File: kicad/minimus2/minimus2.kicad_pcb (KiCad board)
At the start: 2 copper layers, 67.7 x 58.8 mm, 84 parts, among them J1 PROG_SER, J2 LM, J3 LM, Q1 SSM6N58NU_LF, Q2 SSM6N58NU_LF, Q3 DMN3051L, SW1 RESET, SW2 USER_A, SW4 SW_SPDT, U1 LSM6DSRTR, U2 STM32U575CITx, U3 DRV8835, U4 AS5047D, U5 AS5047D, U6 AP2210N-3.3TRG1, U9 AP7370-50FDC

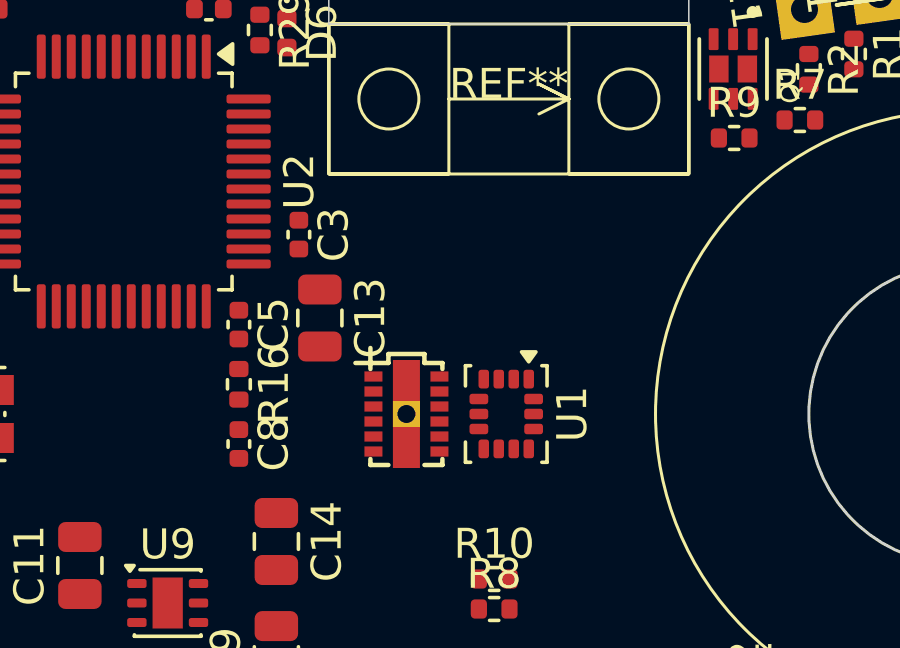
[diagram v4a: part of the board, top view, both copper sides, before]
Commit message: update the motor mounts
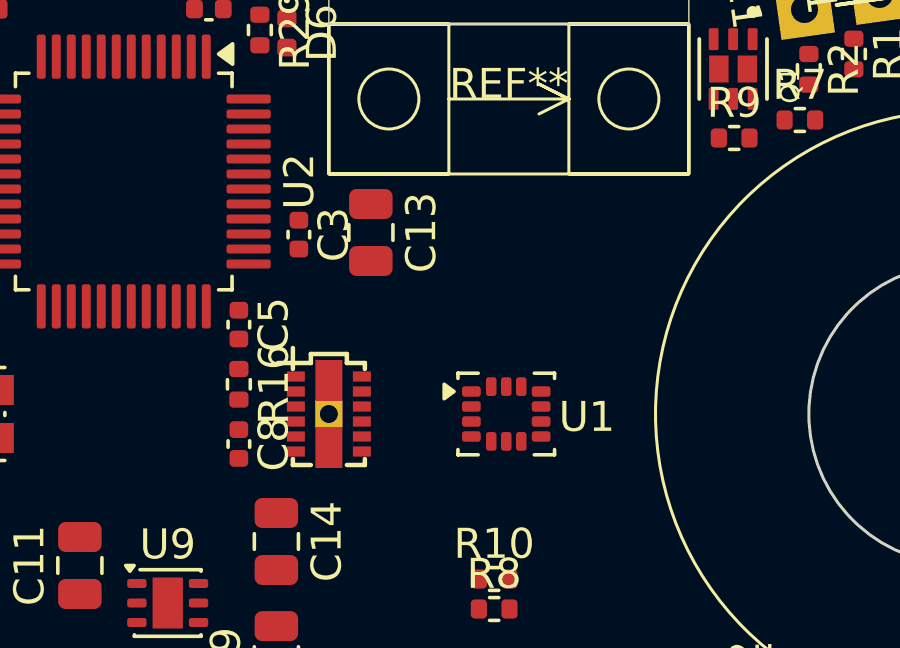
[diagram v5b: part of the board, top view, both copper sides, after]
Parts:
- moved C13 3.32 mm to (95.4, 94.0)
- moved U3 2.58 mm to (94.0, 100.0)
- turned U1 to 0 degrees
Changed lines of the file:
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@@
 		)
 		(embedded_fonts no)
-		(model "${KIPRJMOD}/libraries/minimus.3dshape/MotorMountMK4_TYRE_v4_LHS.step"
+		(model "${KIPRJMOD}/libraries/minimus.3dshape/MotorMountMK4_Thin_LHS.step"
 			(offset
 				(xyz 0 -2.5 0)
@@
 	(footprint "Capacitor_SMD:C_0805_2012Metric"
 		(layer "F.Cu")
-		(at 93.7 96.8 -90)
+		(at 95.4 93.95 -90)
 		(descr "Capacitor SMD 0805 (2012 Metric), square (rectangular) end terminal, IPC-7351 nominal, (Body size source: IPC-SM-782 page 76, https://www.pcb-3d.com/wordpress/wp-content/uploads/ipc-sm-782a_amendment_1_and_2.pdf, https://docs.google.com/spreadsheets/d/1BsfQQcO9C6DZCsRaXUlFlo91Tg2WpOkGARC1WS5S8t0/edit?usp=sharing), generated with kicad-footprint-generator")
 		(tags "capacitor")
@@
 			(stroke
 				(width 0.1)
-				(type default)
+				(type solid)
 			)
 			(layer "F.SilkS")
@@
 		)
 		(embedded_fonts no)
-		(model "${KIPRJMOD}/libraries/minimus.3dshape/MotorMountMK4_TYRE_v4_RHS.step"
+		(model "${KIPRJMOD}/libraries/minimus.3dshape/MotorMountMK4_Thin_RHS.step"
 			(offset
 				(xyz 0 2.5 0)
@@
 	(footprint "Package_LGA:LGA-14_3x2.5mm_P0.5mm_LayoutBorder3x4y"
 		(layer "F.Cu")
-		(at 99.9125 100 -90)
+		(at 99.9125 100)
 		(descr "LGA, 14 Pin (https://www.st.com/resource/en/datasheet/lsm6ds3tr-c.pdf), generated with kicad-footprint-generator ipc_noLead_generator.py")
 		(tags "LGA NoLead")
 		(property "Reference" "U1"
-			(at 0 -2.2 90)
+			(at 2.6875 0.1 0)
 			(layer "F.SilkS")
 			(effects
@@
 		)
 		(property "Value" "LSM6DSRTR"
-			(at 0 2.2 90)
+			(at 0 2.2 0)
 			(layer "F.Fab")
 			(effects
@@
 		)
 		(property "Datasheet" "https://www.st.com/resource/en/datasheet/lsm6ds3tr-c.pdf"
-			(at 0 0 90)
+			(at 0 0 0)
 			(layer "F.Fab")
 			(hide yes)
@@
 		)
 		(property "Description" "I2C/SPI, iNEMO inertial module: always-on 3D accelerometer and 3D gyroscope"
-			(at 0 0 90)
+			(at 0 0 0)
 			(layer "F.Fab")
 			(hide yes)
@@
 		)
 		(property "LCSC" "C784817"
-			(at 0 0 270)
+			(at 0 0 0)
 			(unlocked yes)
 			(layer "F.Fab")
@@
 		)
 		(property "Digikey" "-"
-			(at 0 0 270)
+			(at 0 0 0)
 			(unlocked yes)
 			(layer "F.Fab")
@@
 		(attr smd)
 		(fp_line
-			(start -1.61 1.36)
-			(end -1.61 1.185)
+			(start -1.61 -1.36)
+			(end -0.935 -1.36)
 			(stroke
 				(width 0.12)
@@
 		)
 		(fp_line
-			(start -0.935 1.36)
-			(end -1.61 1.36)
+			(start -1.61 -1.185)
+			(end -1.61 -1.36)
 			(stroke
 				(width 0.12)
@@
 		)
 		(fp_line
-			(start 1.61 1.36)
-			(end 0.935 1.36)
+			(start -1.61 1.36)
+			(end -1.61 1.185)
 			(stroke
 				(width 0.12)
@@
 		)
 		(fp_line
-			(start 1.61 1.185)
-			(end 1.61 1.36)
+			(start -0.935 1.36)
+			(end -1.61 1.36)
 			(stroke
 				(width 0.12)
@@
 		)
 		(fp_line
-			(start -1.61 -1.185)
-			(end -1.61 -1.36)
+			(start 0.935 -1.36)
+			(end 1.61 -1.36)
 			(stroke
 				(width 0.12)
@@
 		)
 		(fp_line
-			(start -1.61 -1.36)
-			(end -0.935 -1.36)
+			(start 1.61 -1.36)
+			(end 1.61 -1.185)
 			(stroke
 				(width 0.12)
@@
 		)
 		(fp_line
-			(start 0.935 -1.36)
-			(end 1.61 -1.36)
+			(start 1.61 1.185)
+			(end 1.61 1.36)
 			(stroke
 				(width 0.12)
@@
 		)
 		(fp_line
-			(start 1.61 -1.36)
-			(end 1.61 -1.185)
+			(start 1.61 1.36)
+			(end 0.935 1.36)
 			(stroke
 				(width 0.12)
@@
 		)
 		(fp_text user "${REFERENCE}"
-			(at 0 0 90)
+			(at 0 0 0)
 			(layer "F.Fab")
 			(effects
@@
 		)
 		(pad "1" smd roundrect
-			(at -1.1625 -0.75 270)
+			(at -1.1625 -0.75)
 			(size 0.625 0.35)
 			(layers "F.Cu" "F.Mask" "F.Paste")
@@
 		)
 		(pad "2" smd roundrect
-			(at -1.1625 -0.25 270)
+			(at -1.1625 -0.25)
 			(size 0.625 0.35)
 			(layers "F.Cu" "F.Mask" "F.Paste")
@@
 		)
 		(pad "3" smd roundrect
-			(at -1.1625 0.25 270)
+			(at -1.1625 0.25)
 			(size 0.625 0.35)
 			(layers "F.Cu" "F.Mask" "F.Paste")
@@
 		)
 		(pad "4" smd roundrect
-			(at -1.1625 0.75 270)
+			(at -1.1625 0.75)
 			(size 0.625 0.35)
 			(layers "F.Cu" "F.Mask" "F.Paste")
@@
 		)
 		(pad "5" smd roundrect
-			(at -0.5 0.9125 270)
+			(at -0.5 0.9125)
 			(size 0.35 0.625)
 			(layers "F.Cu" "F.Mask" "F.Paste")
@@
 		)
 		(pad "6" smd roundrect
-			(at 0 0.9125 270)
+			(at 0 0.9125)
 			(size 0.35 0.625)
 			(layers "F.Cu" "F.Mask" "F.Paste")
@@
 		)
 		(pad "7" smd roundrect
-			(at 0.5 0.9125 270)
+			(at 0.5 0.9125)
 			(size 0.35 0.625)
 			(layers "F.Cu" "F.Mask" "F.Paste")
@@
 		)
 		(pad "8" smd roundrect
-			(at 1.1625 0.75 270)
+			(at 1.1625 0.75)
 			(size 0.625 0.35)
 			(layers "F.Cu" "F.Mask" "F.Paste")
@@
 		)
 		(pad "9" smd roundrect
-			(at 1.1625 0.25 270)
+			(at 1.1625 0.25)
 			(size 0.625 0.35)
 			(layers "F.Cu" "F.Mask" "F.Paste")
@@
 		)
 		(pad "10" smd roundrect
-			(at 1.1625 -0.25 270)
+			(at 1.1625 -0.25)
 			(size 0.625 0.35)
 			(layers "F.Cu" "F.Mask" "F.Paste")
@@
 		)
 		(pad "11" smd roundrect
-			(at 1.1625 -0.75 270)
+			(at 1.1625 -0.75)
 			(size 0.625 0.35)
 			(layers "F.Cu" "F.Mask" "F.Paste")
@@
 		)
 		(pad "12" smd roundrect
-			(at 0.5 -0.9125 270)
+			(at 0.5 -0.9125)
 			(size 0.35 0.625)
 			(layers "F.Cu" "F.Mask" "F.Paste")
@@
 		)
 		(pad "13" smd roundrect
-			(at 0 -0.9125 270)
+			(at 0 -0.9125)
 			(size 0.35 0.625)
 			(layers "F.Cu" "F.Mask" "F.Paste")
@@
 		)
 		(pad "14" smd roundrect
-			(at -0.5 -0.9125 270)
+			(at -0.5 -0.9125)
 			(size 0.35 0.625)
 			(layers "F.Cu" "F.Mask" "F.Paste")
@@
 		(placed yes)
 		(layer "F.Cu")
-		(at 96.585 100 -90)
+		(at 94 100 -90)
 		(property "Reference" "U3"
 			(at 3 -2 90)

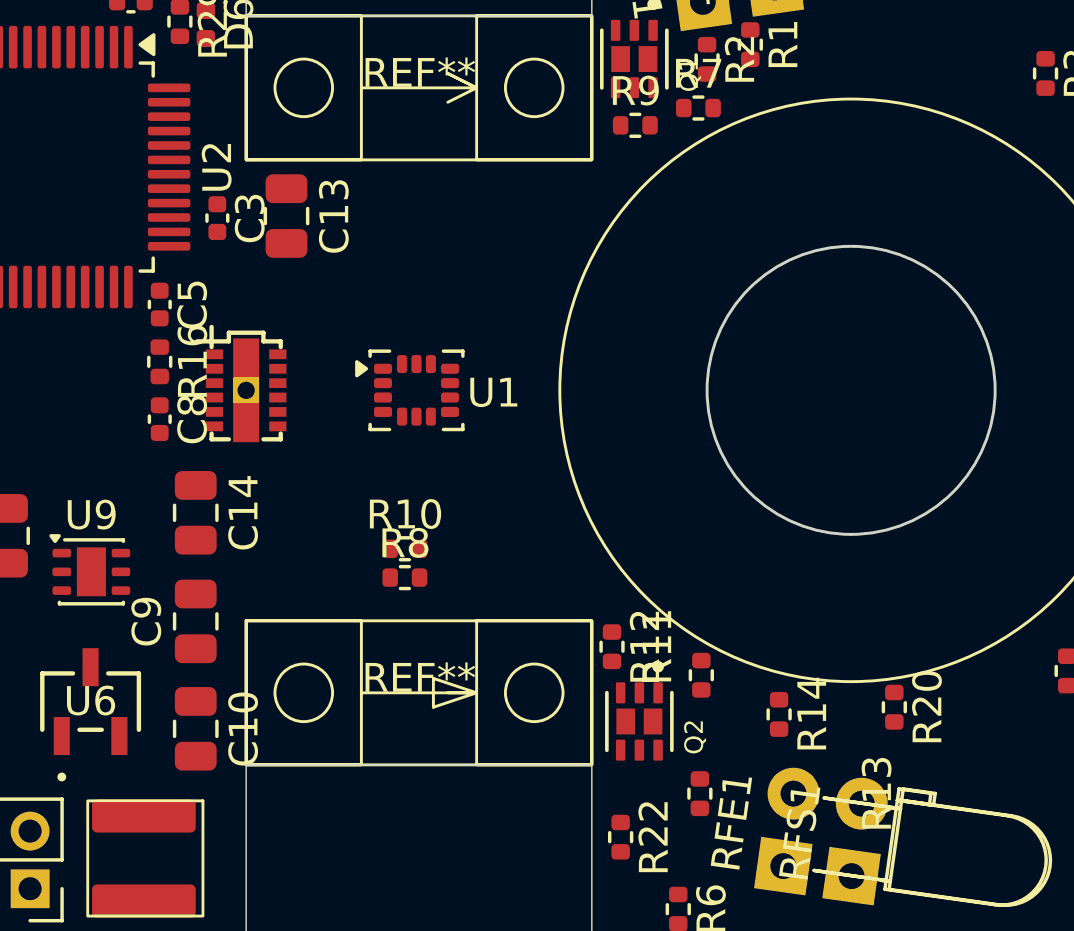
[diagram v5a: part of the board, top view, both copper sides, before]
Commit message: add guideline graduations to silkscreen
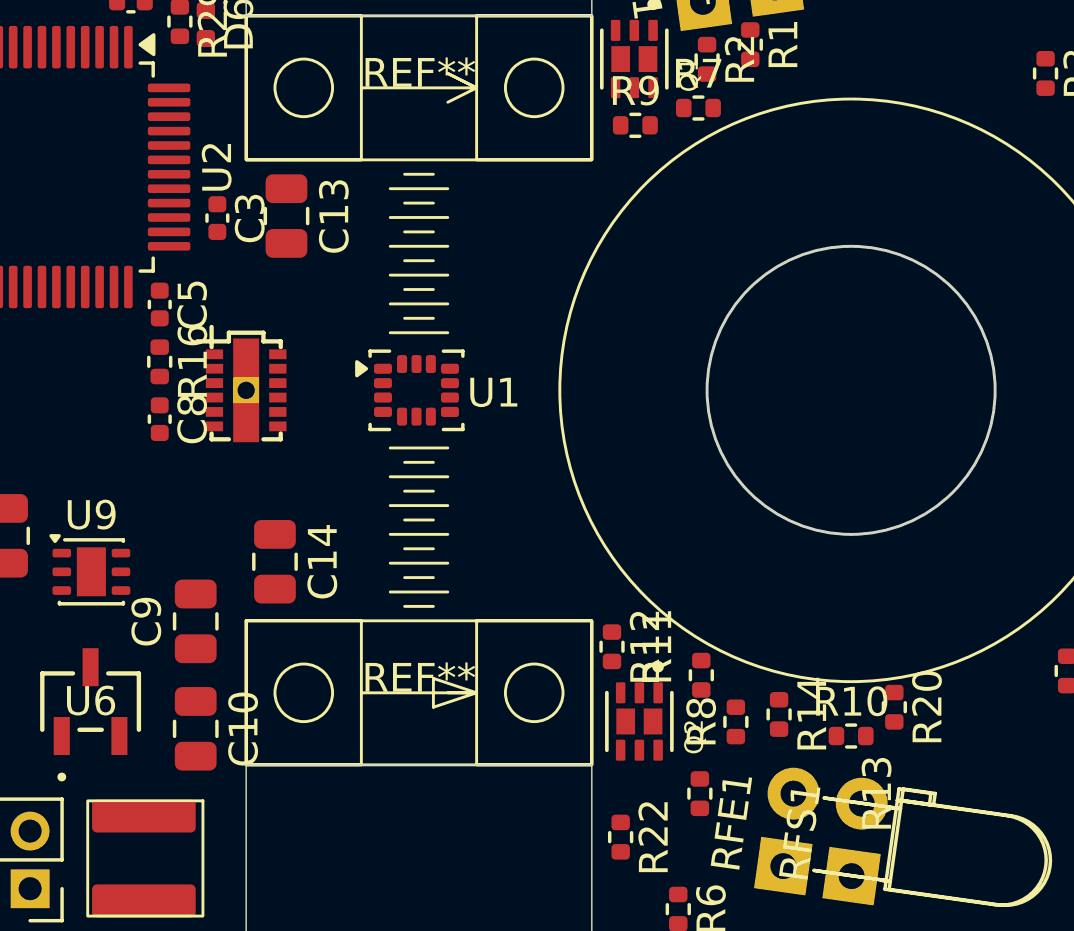
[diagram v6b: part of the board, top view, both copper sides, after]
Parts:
- moved R10 16.8 mm to (115.0, 112.0)
- moved R8 12.5 mm to (111.0, 111.5), turned to 90 degrees
- moved C14 3.23 mm to (95.0, 106.0)
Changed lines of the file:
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@@
 	(footprint "Capacitor_SMD:C_0805_2012Metric"
 		(layer "F.Cu")
-		(at 92.25 104.25 -90)
+		(at 95 105.95 -90)
 		(descr "Capacitor SMD 0805 (2012 Metric), square (rectangular) end terminal, IPC-7351 nominal, (Body size source: IPC-SM-782 page 76, https://www.pcb-3d.com/wordpress/wp-content/uploads/ipc-sm-782a_amendment_1_and_2.pdf, https://docs.google.com/spreadsheets/d/1BsfQQcO9C6DZCsRaXUlFlo91Tg2WpOkGARC1WS5S8t0/edit?usp=sharing), generated with kicad-footprint-generator")
 		(tags "capacitor")
@@
 	(footprint "Resistor_SMD:R_0402_1005Metric"
 		(layer "F.Cu")
-		(at 99.51 106.5)
+		(at 111 111.51 90)
 		(descr "Resistor SMD 0402 (1005 Metric), square (rectangular) end terminal, IPC-7351 nominal, (Body size source: IPC-SM-782 page 72, https://www.pcb-3d.com/wordpress/wp-content/uploads/ipc-sm-782a_amendment_1_and_2.pdf), generated with kicad-footprint-generator")
 		(tags "resistor")
 		(property "Reference" "R8"
-			(at 0 -1.17 0)
+			(at 0 -1.17 90)
 			(layer "F.SilkS")
 			(effects
@@
 		)
 		(property "Value" "1k0"
-			(at 0 1.17 0)
+			(at 0 1.17 90)
 			(layer "F.Fab")
 			(effects
@@
 		)
 		(property "Datasheet" "~"
-			(at 0 0 0)
+			(at 0 0 90)
 			(layer "F.Fab")
 			(hide yes)
@@
 		)
 		(property "Description" "Resistor, small symbol"
-			(at 0 0 0)
+			(at 0 0 90)
 			(layer "F.Fab")
 			(hide yes)
@@
 		)
 		(property "LCSC" "-"
-			(at 0 0 0)
+			(at 0 0 90)
 			(unlocked yes)
 			(layer "F.Fab")
@@
 		)
 		(property "Digikey" "-"
-			(at 0 0 0)
+			(at 0 0 90)
 			(unlocked yes)
 			(layer "F.Fab")
@@
 		)
 		(fp_line
-			(start -0.93 -0.47)
-			(end 0.93 -0.47)
+			(start 0.93 -0.47)
+			(end 0.93 0.47)
 			(stroke
 				(width 0.05)
@@
 		)
 		(fp_line
-			(start -0.93 0.47)
-			(end -0.93 -0.47)
+			(start -0.93 -0.47)
+			(end 0.93 -0.47)
 			(stroke
 				(width 0.05)
@@
 		)
 		(fp_line
-			(start 0.93 -0.47)
-			(end 0.93 0.47)
+			(start 0.93 0.47)
+			(end -0.93 0.47)
 			(stroke
 				(width 0.05)
@@
 		)
 		(fp_line
-			(start 0.93 0.47)
-			(end -0.93 0.47)
+			(start -0.93 0.47)
+			(end -0.93 -0.47)
 			(stroke
 				(width 0.05)
@@
 		)
 		(fp_line
-			(start -0.525 -0.27)
-			(end 0.525 -0.27)
+			(start 0.525 -0.27)
+			(end 0.525 0.27)
 			(stroke
 				(width 0.1)
@@
 		)
 		(fp_line
-			(start -0.525 0.27)
-			(end -0.525 -0.27)
+			(start -0.525 -0.27)
+			(end 0.525 -0.27)
 			(stroke
 				(width 0.1)
@@
 		)
 		(fp_line
-			(start 0.525 -0.27)
-			(end 0.525 0.27)
+			(start 0.525 0.27)
+			(end -0.525 0.27)
 			(stroke
 				(width 0.1)
@@
 		)
 		(fp_line
-			(start 0.525 0.27)
-			(end -0.525 0.27)
+			(start -0.525 0.27)
+			(end -0.525 -0.27)
 			(stroke
 				(width 0.1)
@@
 		)
 		(fp_text user "${REFERENCE}"
-			(at 0 0 0)
+			(at 0 0 90)
 			(layer "F.Fab")
 			(effects
@@
 		)
 		(pad "1" smd roundrect
-			(at -0.51 0)
+			(at -0.51 0 90)
 			(size 0.54 0.64)
 			(layers "F.Cu" "F.Mask" "F.Paste")
@@
 		)
 		(pad "2" smd roundrect
-			(at 0.51 0)
+			(at 0.51 0 90)
 			(size 0.54 0.64)
 			(layers "F.Cu" "F.Mask" "F.Paste")
@@
 	(footprint "Resistor_SMD:R_0402_1005Metric"
 		(layer "F.Cu")
-		(at 99.51 105.5)
+		(at 115 112)
 		(descr "Resistor SMD 0402 (1005 Metric), square (rectangular) end terminal, IPC-7351 nominal, (Body size source: IPC-SM-782 page 72, https://www.pcb-3d.com/wordpress/wp-content/uploads/ipc-sm-782a_amendment_1_and_2.pdf), generated with kicad-footprint-generator")
 		(tags "resistor")
@@
 		)
 	)
+	(gr_line
+		(start 99 103)
+		(end 101 103)
+		(stroke
+			(width 0.1)
+			(type default)
+		)
+		(layer "F.SilkS")
+	)
+	(gr_line
+		(start 99.5 93.5)
+		(end 100.5 93.5)
+		(stroke
+			(width 0.1)
+			(type default)
+		)
+		(layer "F.SilkS")
+	)
+	(gr_line
+		(start 99 94)
+		(end 101 94)
+		(stroke
+			(width 0.1)
+			(type default)
+		)
+		(layer "F.SilkS")
+	)
+	(gr_line
+		(start 99.5 105.5)
+		(end 100.5 105.5)
+		(stroke
+			(width 0.1)
+			(type default)
+		)
+		(layer "F.SilkS")
+	)
+	(gr_line
+		(start 99 106)
+		(end 101 106)
+		(stroke
+			(width 0.1)
+			(type default)
+		)
+		(layer "F.SilkS")
+	)
+	(gr_line
+		(start 99 107)
+		(end 101 107)
+		(stroke
+			(width 0.1)
+			(type default)
+		)
+		(layer "F.SilkS")
+	)
+	(gr_line
+		(start 99.5 107.5)
+		(end 100.5 107.5)
+		(stroke
+			(width 0.1)
+			(type default)
+		)
+		(layer "F.SilkS")
+	)
+	(gr_line
+		(start 99 102)
+		(end 101 102)
+		(stroke
+			(width 0.1)
+			(type default)
+		)
+		(layer "F.SilkS")
+	)
+	(gr_line
+		(start 99 96)
+		(end 101 96)
+		(stroke
+			(width 0.1)
+			(type default)
+		)
+		(layer "F.SilkS")
+	)
+	(gr_line
+		(start 99 97)
+		(end 101 97)
+		(stroke
+			(width 0.1)
+			(type default)
+		)
+		(layer "F.SilkS")
+	)
+	(gr_line
+		(start 99.5 96.5)
+		(end 100.5 96.5)
+		(stroke
+			(width 0.1)
+			(type default)
+		)
+		(layer "F.SilkS")
+	)
+	(gr_line
+		(start 99.5 102.5)
+		(end 100.5 102.5)
+		(stroke
+			(width 0.1)
+			(type default)
+		)
+		(layer "F.SilkS")
+	)
+	(gr_line
+		(start 99.5 97.5)
+		(end 100.5 97.5)
+		(stroke
+			(width 0.1)
+			(type default)
+		)
+		(layer "F.SilkS")
+	)
+	(gr_line
+		(start 99.5 92.5)
+		(end 100.5 92.5)
+		(stroke
+			(width 0.1)
+			(type default)
+		)
+		(layer "F.SilkS")
+	)
+	(gr_line
+		(start 99.5 106.5)
+		(end 100.5 106.5)
+		(stroke
+			(width 0.1)
+			(type default)
+		)
+		(layer "F.SilkS")
+	)
+	(gr_line
+		(start 99.5 103.5)
+		(end 100.5 103.5)
+		(stroke
+			(width 0.1)
+			(type default)
+		)
+		(layer "F.SilkS")
+	)
+	(gr_line
+		(start 99 98)
+		(end 101 98)
+		(stroke
+			(width 0.1)
+			(type default)
+		)
+		(layer "F.SilkS")
+	)
+	(gr_line
+		(start 99.5 104.5)
+		(end 100.5 104.5)
+		(stroke
+			(width 0.1)
+			(type default)
+		)
+		(layer "F.SilkS")
+	)
+	(gr_line
+		(start 99 104)
+		(end 101 104)
+		(stroke
+			(width 0.1)
+			(type default)
+		)
+		(layer "F.SilkS")
+	)
+	(gr_line
+		(start 99 95)
+		(end 101 95)
+		(stroke
+			(width 0.1)
+			(type default)
+		)
+		(layer "F.SilkS")
+	)
+	(gr_line
+		(start 99.5 94.5)
+		(end 100.5 94.5)
+		(stroke
+			(width 0.1)
+			(type default)
+		)
+		(layer "F.SilkS")
+	)
+	(gr_line
+		(start 99 105)
+		(end 101 105)
+		(stroke
+			(width 0.1)
+			(type default)
+		)
+		(layer "F.SilkS")
+	)
+	(gr_line
+		(start 99.5 95.5)
+		(end 100.5 95.5)
+		(stroke
+			(width 0.1)
+			(type default)
+		)
+		(layer "F.SilkS")
+	)
 	(gr_circle
 		(center 115 100)
@@
 		(layer "F.SilkS")
 	)
+	(gr_line
+		(start 99 93)
+		(end 101 93)
+		(stroke
+			(width 0.1)
+			(type default)
+		)
+		(layer "F.SilkS")
+	)

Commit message: populate the encoder carriers
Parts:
- moved R33 42.1 mm to (67.0, 89.9), turned to -90 degrees
- moved R18 41.9 mm to (67.0, 98.5), turned to -90 degrees
- moved LS1 40.5 mm to (88.5, 100.0)
- moved R23 40.5 mm to (85.5, 100.8)
- moved R28 40.5 mm to (85.5, 99.0)
- moved U5 40.2 mm to (70.5, 101.5), turned to -90 degrees
- moved R30 38.7 mm to (67.0, 104.5), turned to -90 degrees
- moved R32 37.6 mm to (67.0, 91.9), turned to -90 degrees
- moved R17 37.1 mm to (67.0, 102.5), turned to -90 degrees
- moved U4 36.6 mm to (70.5, 93.0), turned to 90 degrees
- moved C15 36.0 mm to (67.0, 100.5), turned to -90 degrees
- moved C12 32.5 mm to (67.0, 93.9), turned to -90 degrees
- moved TP1 31.0 mm to (84.0, 83.5)
- moved R15 28.7 mm to (67.0, 95.9), turned to -90 degrees
- moved Q2 17.3 mm to (124.5, 115.5)
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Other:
- board size 67.7 x 58.8 mm -> 69 x 38 mm
